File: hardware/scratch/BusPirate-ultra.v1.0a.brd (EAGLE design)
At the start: 100 x 50 mm, 136 parts, among them IC1 IC_MEM_23LC1024, IC10 IC_BUFF_SN74LVC1T45DBV, IC11 IC_BUFF_SN74LVC1T45DBV, IC12 74LVC1G07DBV, IC13 IC_BUFF_SN74LVC1T45DBV, IC14 IC_BL1551, IC15 IC_BL1551, IC16 74HCT4066PW, IC2 IC_MEM_23LC1024, IC3 IC_74AC573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

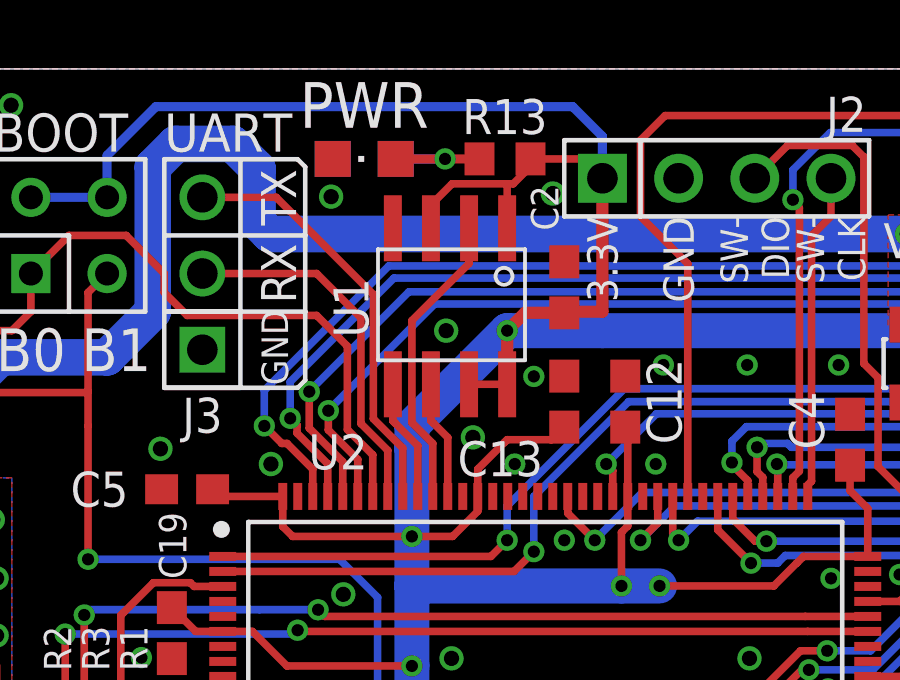
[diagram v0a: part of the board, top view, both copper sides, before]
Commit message: flash CS now connected to STM's PG15
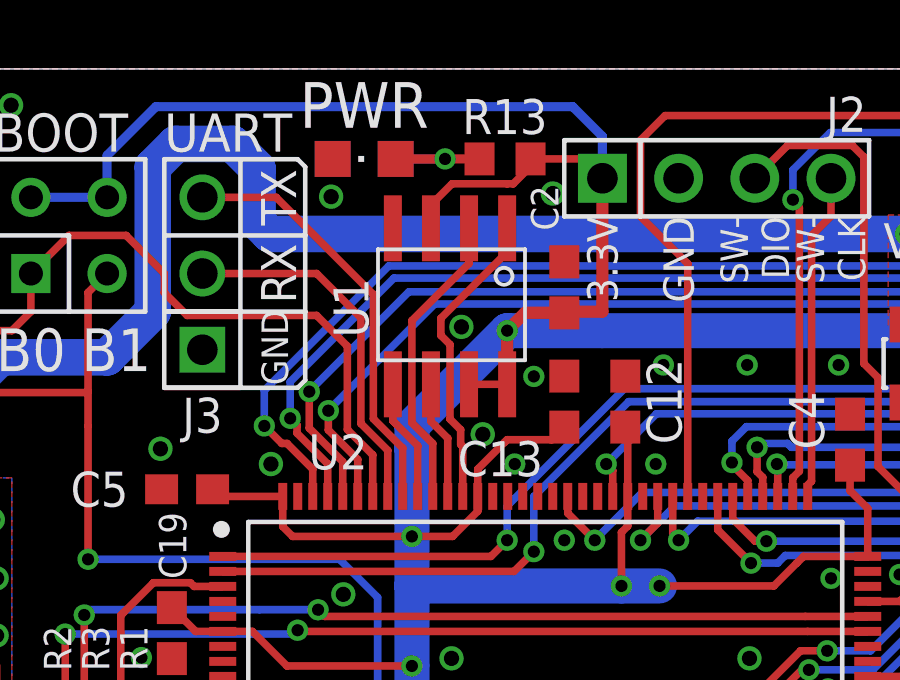
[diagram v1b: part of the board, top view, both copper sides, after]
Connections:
- removed net N$61: U2.132
- new net FLASH_CS: U1.1, U2.132
- net 3V3: no longer U1.1
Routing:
- net FLASH_CS: track 0.00 -> 10.2 mm
- net 3V3: track 513.8 -> 512.4 mm
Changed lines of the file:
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@@
 <setting verticaltext="up"/>
 </settings>
-<grid distance="25" unitdist="mil" unit="mil" style="lines" multiple="1" display="no" altdistance="5" altunitdist="mil" altunit="mil"/>
+<grid distance="25" unitdist="mil" unit="mil" style="lines" multiple="1" display="no" altdistance="1" altunitdist="mil" altunit="mil"/>
 <layers>
 <layer number="1" name="Top" color="4" fill="1" visible="yes" active="yes"/>
@@
 <via x="3.2766" y="41.2976" extent="1-16" drill="0.508"/>
 <via x="18.8976" y="45.7426" extent="1-16" drill="0.508"/>
-<via x="23.622" y="37.719" extent="1-16" drill="0.508"/>
+<via x="23.9522" y="37.8206" extent="1-16" drill="0.508"/>
 <via x="29.972" y="40.132" extent="1-16" drill="0.4064"/>
 <via x="25.654" y="39.751" extent="1-16" drill="0.4064"/>
@@
 <via x="54.0004" y="32.8422" extent="1-16" drill="0.4064"/>
 <via x="26.67" y="34.29" extent="1-16" drill="0.4064"/>
-<via x="22.733" y="41.275" extent="1-16" drill="0.508"/>
+<via x="23.241" y="41.402" extent="1-16" drill="0.508"/>
 <via x="26.289" y="45.847" extent="1-16" drill="0.508"/>
 <via x="13.208" y="37.338" extent="1-16" drill="0.508"/>
@@
 <wire x1="26.67" y1="41.87" x2="26.71" y2="41.91" width="0.4064" layer="1"/>
 <wire x1="26.71" y1="41.91" x2="27.94" y2="41.91" width="0.4064" layer="1"/>
-<contactref element="U1" pad="1"/>
-<wire x1="24.765" y1="44.6878" x2="24.765" y2="46.1706" width="0.254" layer="1"/>
 </signal>
 <signal name="N$7">
@@
 <signal name="FLASH_SCK">
 <contactref element="U2" pad="133"/>
-<wire x1="22.785" y1="35.75" x2="22.785" y2="37.715" width="0.254" layer="1"/>
-<wire x1="22.785" y1="37.715" x2="22.3125" y2="38.1875" width="0.254" layer="1"/>
+<wire x1="22.785" y1="35.75" x2="22.785" y2="37.6896" width="0.254" layer="1"/>
+<wire x1="22.785" y1="37.6896" x2="22.3633" y2="38.1113" width="0.254" layer="1"/>
 <contactref element="U1" pad="6"/>
-<wire x1="22.3125" y1="38.1875" x2="22.225" y2="38.275" width="0.254" layer="1"/>
-<wire x1="22.3125" y1="38.1875" x2="22.225" y2="38.275" width="0.254" layer="1"/>
-<wire x1="22.225" y1="38.275" x2="22.225" y2="39.4878" width="0.254" layer="1"/>
+<wire x1="22.3633" y1="38.1113" x2="22.225" y2="38.2496" width="0.254" layer="1"/>
+<wire x1="22.225" y1="38.2496" x2="22.225" y2="39.4878" width="0.254" layer="1"/>
 </signal>
 <signal name="FLASH_MISO">
@@
 <contactref element="U2" pad="135"/>
 <wire x1="21.785" y1="35.75" x2="21.785" y2="37.44039375" width="0.254" layer="1"/>
-<wire x1="21.785" y1="37.44039375" x2="21.040196875" y2="38.185196875" width="0.254" layer="1"/>
+<wire x1="21.785" y1="37.44039375" x2="21.065596875" y2="38.159796875" width="0.254" layer="1"/>
 <contactref element="U1" pad="5"/>
-<wire x1="21.040196875" y1="38.185196875" x2="20.955" y2="38.27039375" width="0.254" layer="1"/>
-<wire x1="21.040196875" y1="38.185196875" x2="20.955" y2="38.27039375" width="0.254" layer="1"/>
+<wire x1="21.065596875" y1="38.159796875" x2="20.955" y2="38.27039375" width="0.254" layer="1"/>
 <wire x1="20.955" y1="38.27039375" x2="20.955" y2="39.4878" width="0.254" layer="1"/>
 </signal>
@@
 <contactref element="U2" pad="129"/>
 </signal>
-<signal name="N$61">
-<contactref element="U2" pad="132"/>
-</signal>
 <signal name="MCU_AUX2">
 <contactref element="U3" pad="136"/>
@@
 <wire x1="46.736" y1="16.002" x2="46.736" y2="16.04066875" width="0.254" layer="16"/>
 </signal>
+<signal name="FLASH_CS">
+<contactref element="U1" pad="1"/>
+<contactref element="U2" pad="132"/>
+<wire x1="22.5552" y1="41.68606875" x2="22.5552" y2="41.11793125" width="0.254" layer="1"/>
+<wire x1="24.765" y1="44.6878" x2="24.765" y2="43.89586875" width="0.254" layer="1"/>
+<wire x1="22.86" y1="40.81313125" x2="22.5552" y2="41.11793125" width="0.254" layer="1"/>
+<wire x1="24.765" y1="43.89586875" x2="22.5552" y2="41.68606875" width="0.254" layer="1"/>
+<wire x1="23.285" y1="35.75" x2="23.285" y2="37.41633125" width="0.254" layer="1"/>
+<wire x1="23.285" y1="37.41633125" x2="23.2156" y2="37.48573125" width="0.254" layer="1"/>
+<wire x1="23.2156" y1="37.48573125" x2="23.2156" y2="37.97206875" width="0.254" layer="1"/>
+<wire x1="23.2156" y1="37.97206875" x2="22.86" y2="38.32766875" width="0.254" layer="1"/>
+<wire x1="22.86" y1="38.32766875" x2="22.86" y2="40.81313125" width="0.254" layer="1"/>
+</signal>
 </signals>
